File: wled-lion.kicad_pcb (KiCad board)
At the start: 2 copper layers, 49.9 x 11.7 mm, 9 parts, among them J1 ESP, J3 Neo pixels, J5 Power in, SW1 Button, U1 AMS1117-3.3

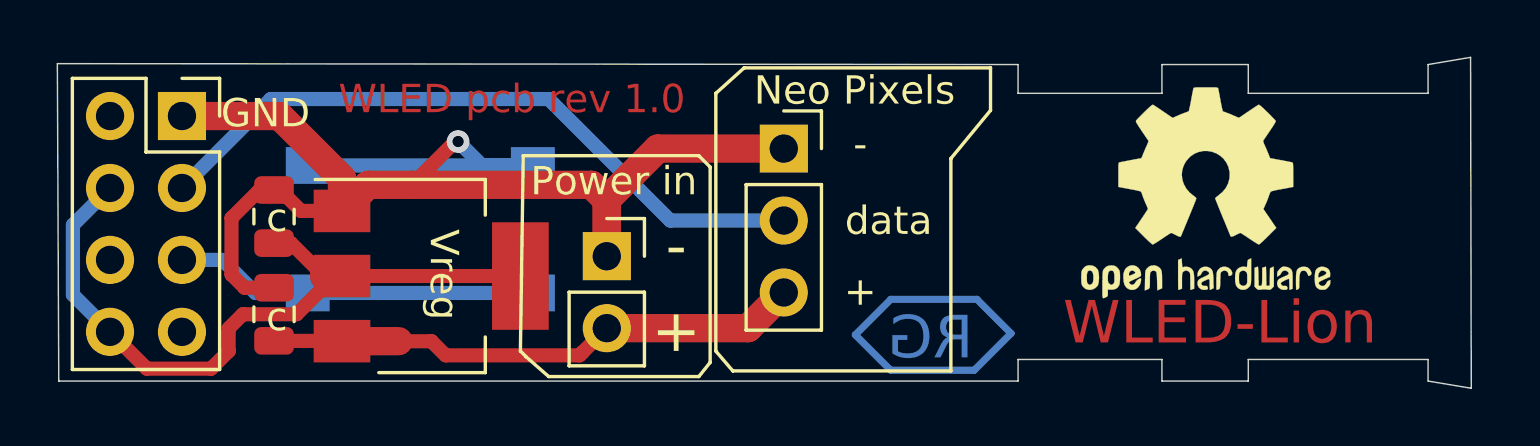
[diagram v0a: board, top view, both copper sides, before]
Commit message: made text larger, no longer open herdware
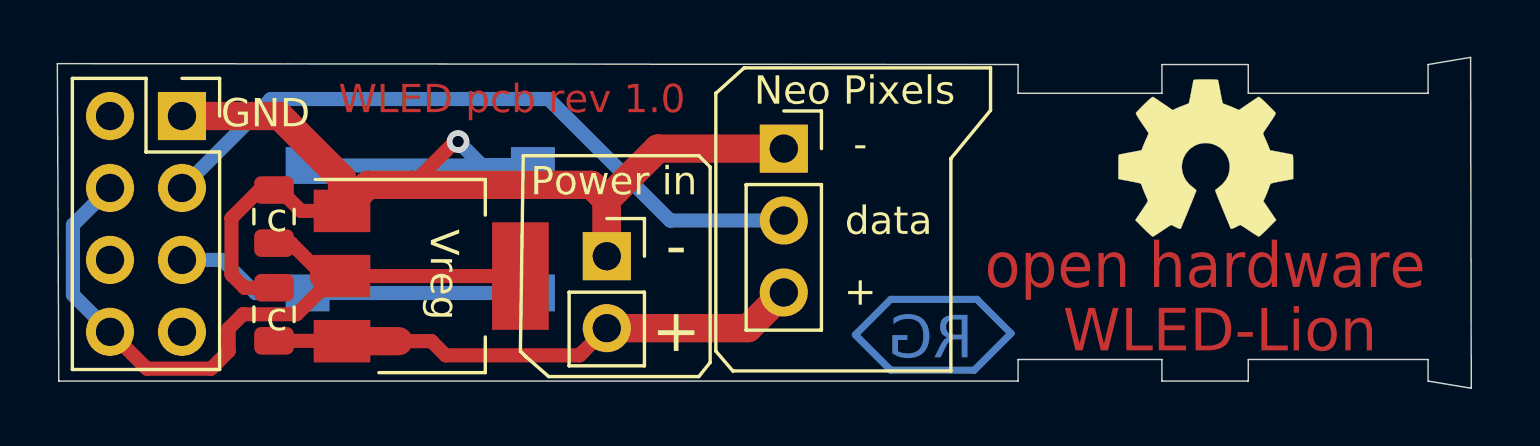
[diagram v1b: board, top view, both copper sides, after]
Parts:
- moved REF** 0.28 mm to (189.0, 88.8)
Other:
- board text added: "open hardware"
